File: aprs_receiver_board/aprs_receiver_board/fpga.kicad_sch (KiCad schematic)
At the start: 28 parts, among them J2 Conn_02x10_Top_Bottom, SW1 SW_SPDT, SW2 SW_DIP_x04, U3 T20Q100F3C3, U5 ADC121S021, X1 ECS-2520MV-xxx-xx

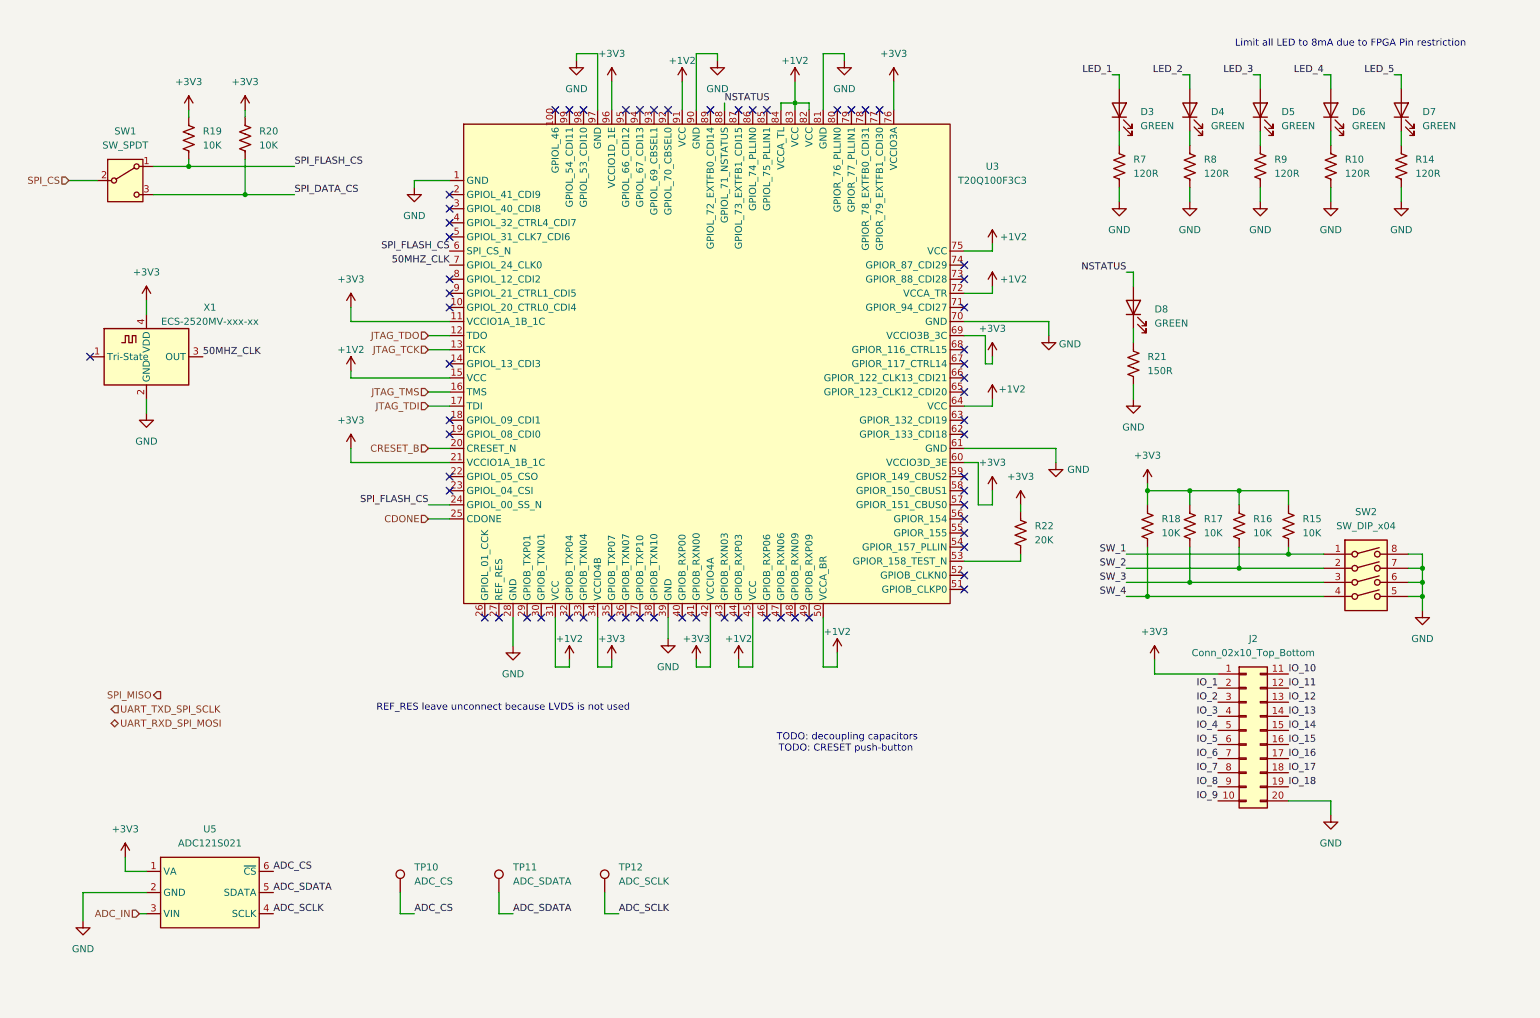
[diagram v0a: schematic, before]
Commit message: Add decoupling capacitor and IO connectors
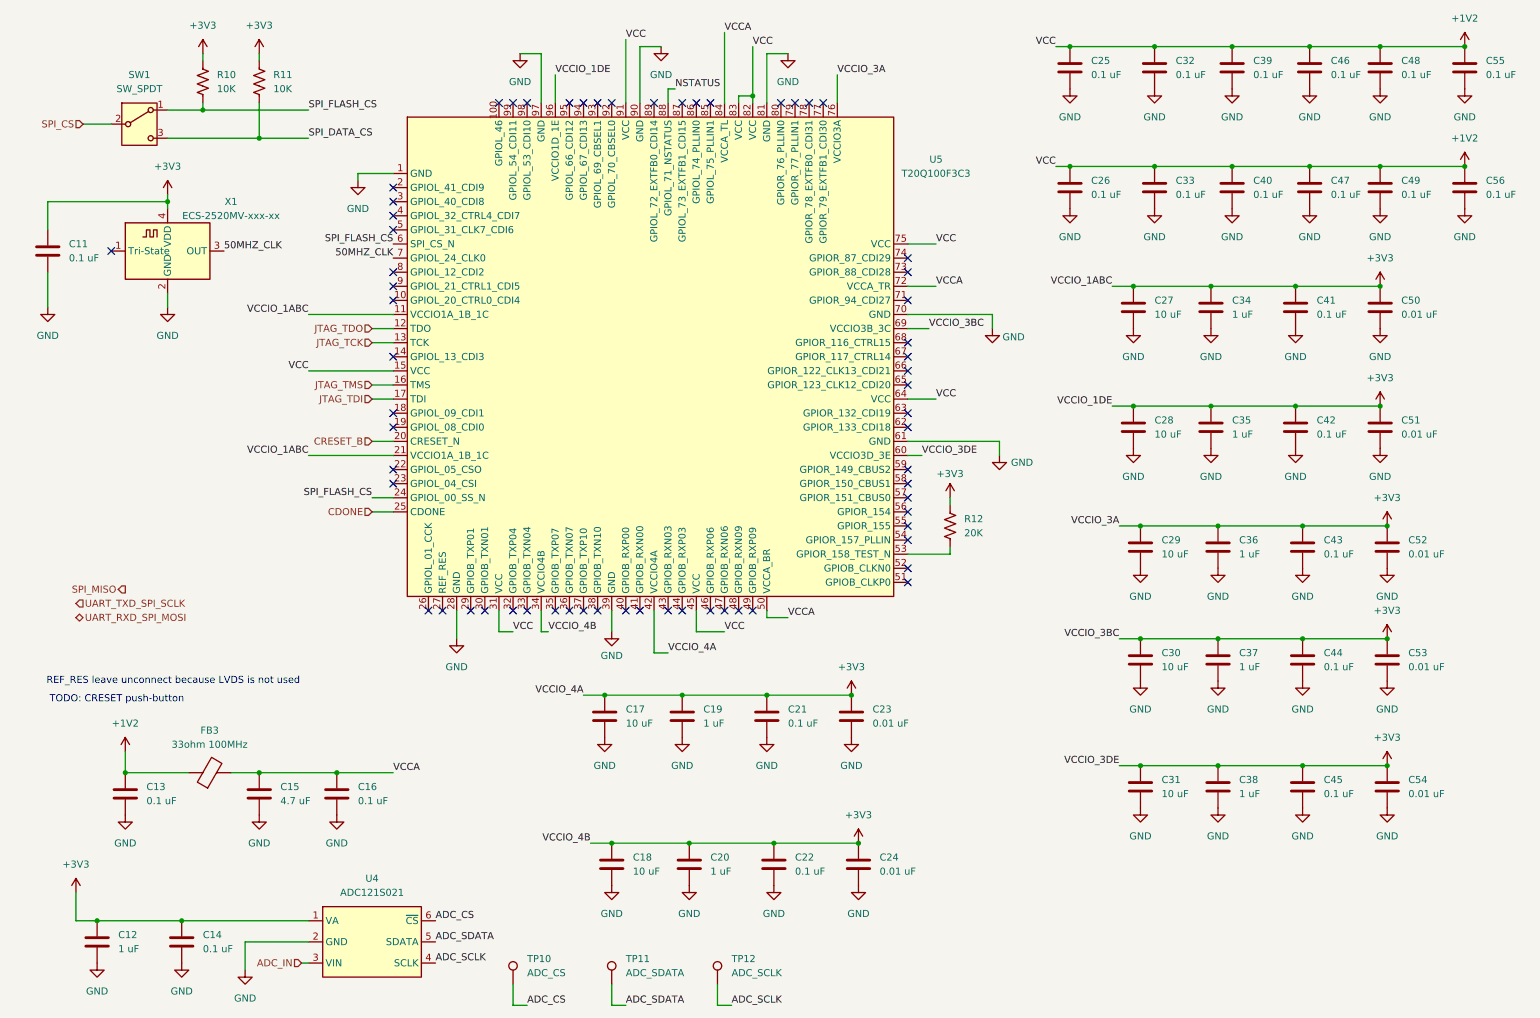
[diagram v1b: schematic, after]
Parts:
- removed D3, D4, D5, D6, D7, D8: GREEN, symbol Device:LED
- removed J2: Conn_02x10_Top_Bottom, symbol Connector_Generic:Conn_02x10_Top_Bottom
- removed R10, R14, R7, R8, R9: 120R, symbol Device:R_US
- removed R15, R16, R17, R18: 10K, symbol Device:R_US
- removed R21: 150R, symbol Device:R_US
- removed SW2: SW_DIP_x04, symbol Switch:SW_DIP_x04
- added C11, C13, C14, C16, C21, C22, C25, C26, C32, C33, C39, C40, C41, C42, C43, C44, C45, C46, C47, C48, C49, C55, C56: 0.1 uF, Capacitor_SMD:C_0805_2012Metric_Pad1.18x1.45mm_HandSolder, symbol Device:C
- added C12, C19, C20, C34, C35, C36, C37, C38: 1 uF, Capacitor_SMD:C_0805_2012Metric_Pad1.18x1.45mm_HandSolder, symbol Device:C
- added C15: 4.7 uF, Capacitor_SMD:C_0805_2012Metric_Pad1.18x1.45mm_HandSolder, symbol Device:C
- added C17, C18, C27, C28, C29, C30, C31: 10 uF, Capacitor_SMD:C_0805_2012Metric_Pad1.18x1.45mm_HandSolder, symbol Device:C
- added C23, C24, C50, C51, C52, C53, C54: 0.01 uF, Capacitor_SMD:C_0805_2012Metric_Pad1.18x1.45mm_HandSolder, symbol Device:C
- added FB3: 33ohm 100MHz, Resistor_SMD:R_0805_2012Metric_Pad1.20x1.40mm_HandSolder, symbol Device:FerriteBead
- R10: renamed from R19; footprint (none) -> Resistor_SMD:R_0805_2012Metric_Pad1.20x1.40mm_HandSolder
- R11: renamed from R20; footprint (none) -> Resistor_SMD:R_0805_2012Metric_Pad1.20x1.40mm_HandSolder
- R12: renamed from R22; footprint (none) -> Resistor_SMD:R_0805_2012Metric_Pad1.20x1.40mm_HandSolder
- TP10, TP11, TP12: footprint (none) -> TestPoint:TestPoint_Keystone_5000-5004_Miniature
- renumbered U5 to U4, U3 to U5
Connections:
- net +1V2: now also C13.1, C25.1, C26.1, C32.1, C33.1, C39.1, C40.1, C46.1, C47.1, C48.1, C49.1, C55.1, C56.1, FB3.1; no longer U5.50 (VCCA_BR), U5.72 (VCCA_TR), U5.84 (VCCA_TL)
- net +3V3: now also C11.1, C12.1, C14.1, C17.1, C18.1, C19.1, C20.1, C21.1, C22.1, C23.1, C24.1, C27.1, C28.1, C29.1, C30.1, C31.1, C34.1, C35.1, C36.1, C37.1, C38.1, C41.1, C42.1, C43.1, C44.1, C45.1, C50.1, C51.1, C52.1, C53.1, C54.1
- net GND: now also C11.2, C12.2, C13.2, C14.2, C15.2, C16.2, C17.2, C18.2, C19.2, C20.2, C21.2, C22.2, C23.2, C24.2, C25.2, C26.2, C27.2, C28.2, C29.2, C30.2, C31.2, C32.2, C33.2, C34.2, C35.2, C36.2, C37.2, C38.2, C39.2, C40.2, C41.2, C42.2, C43.2, C44.2, C45.2, C46.2, C47.2, C48.2, C49.2, C50.2, C51.2, C52.2, C53.2, C54.2, C55.2, C56.2
- new net VCCA: C15.1, C16.1, FB3.2, U5.50 (VCCA_BR), U5.72 (VCCA_TR), U5.84 (VCCA_TL)
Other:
- note removed: "Limit all LED to 8mA due to FPGA Pin restriction"
- note removed: "TODO: decoupling capacitors"
- moved on the sheet: R10, R11, R12, SW1, TP10, TP11, TP12, U4, U5, X1
